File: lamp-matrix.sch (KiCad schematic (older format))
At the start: 0 parts

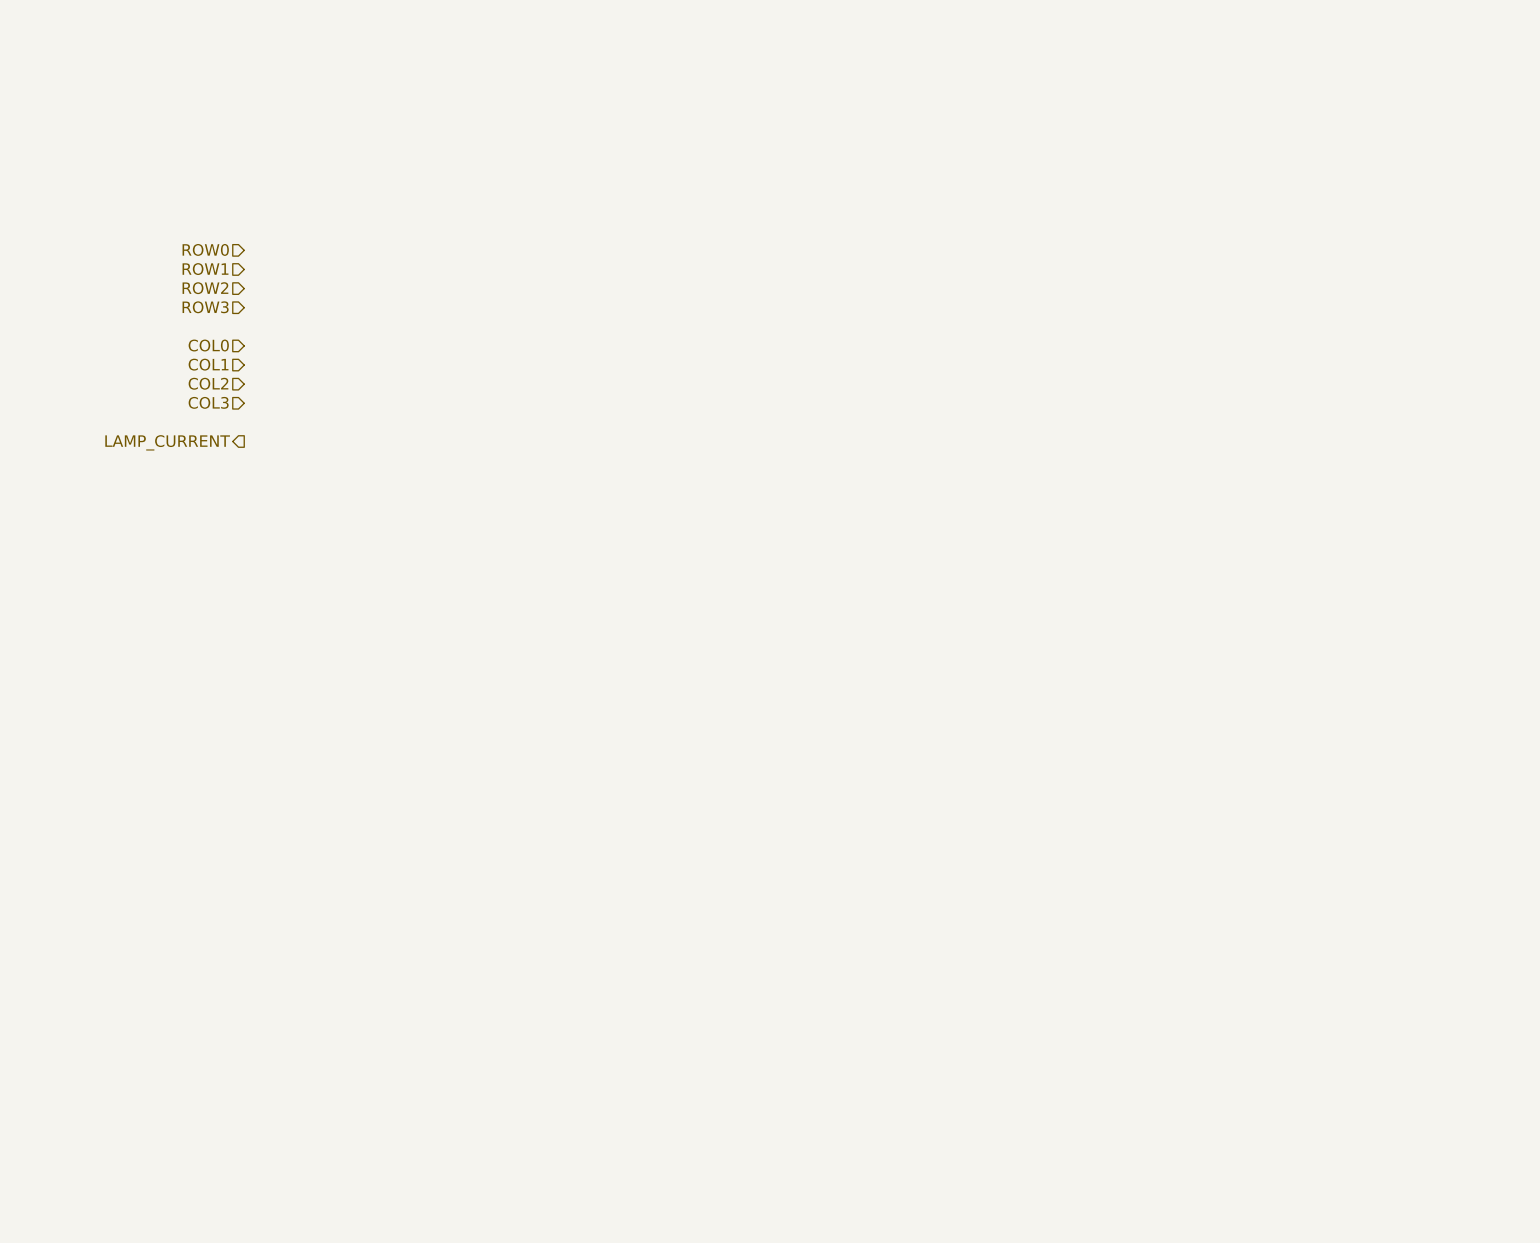
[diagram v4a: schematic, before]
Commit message: Fixed switch matrix to match Mike's sketches Added lamp matrix
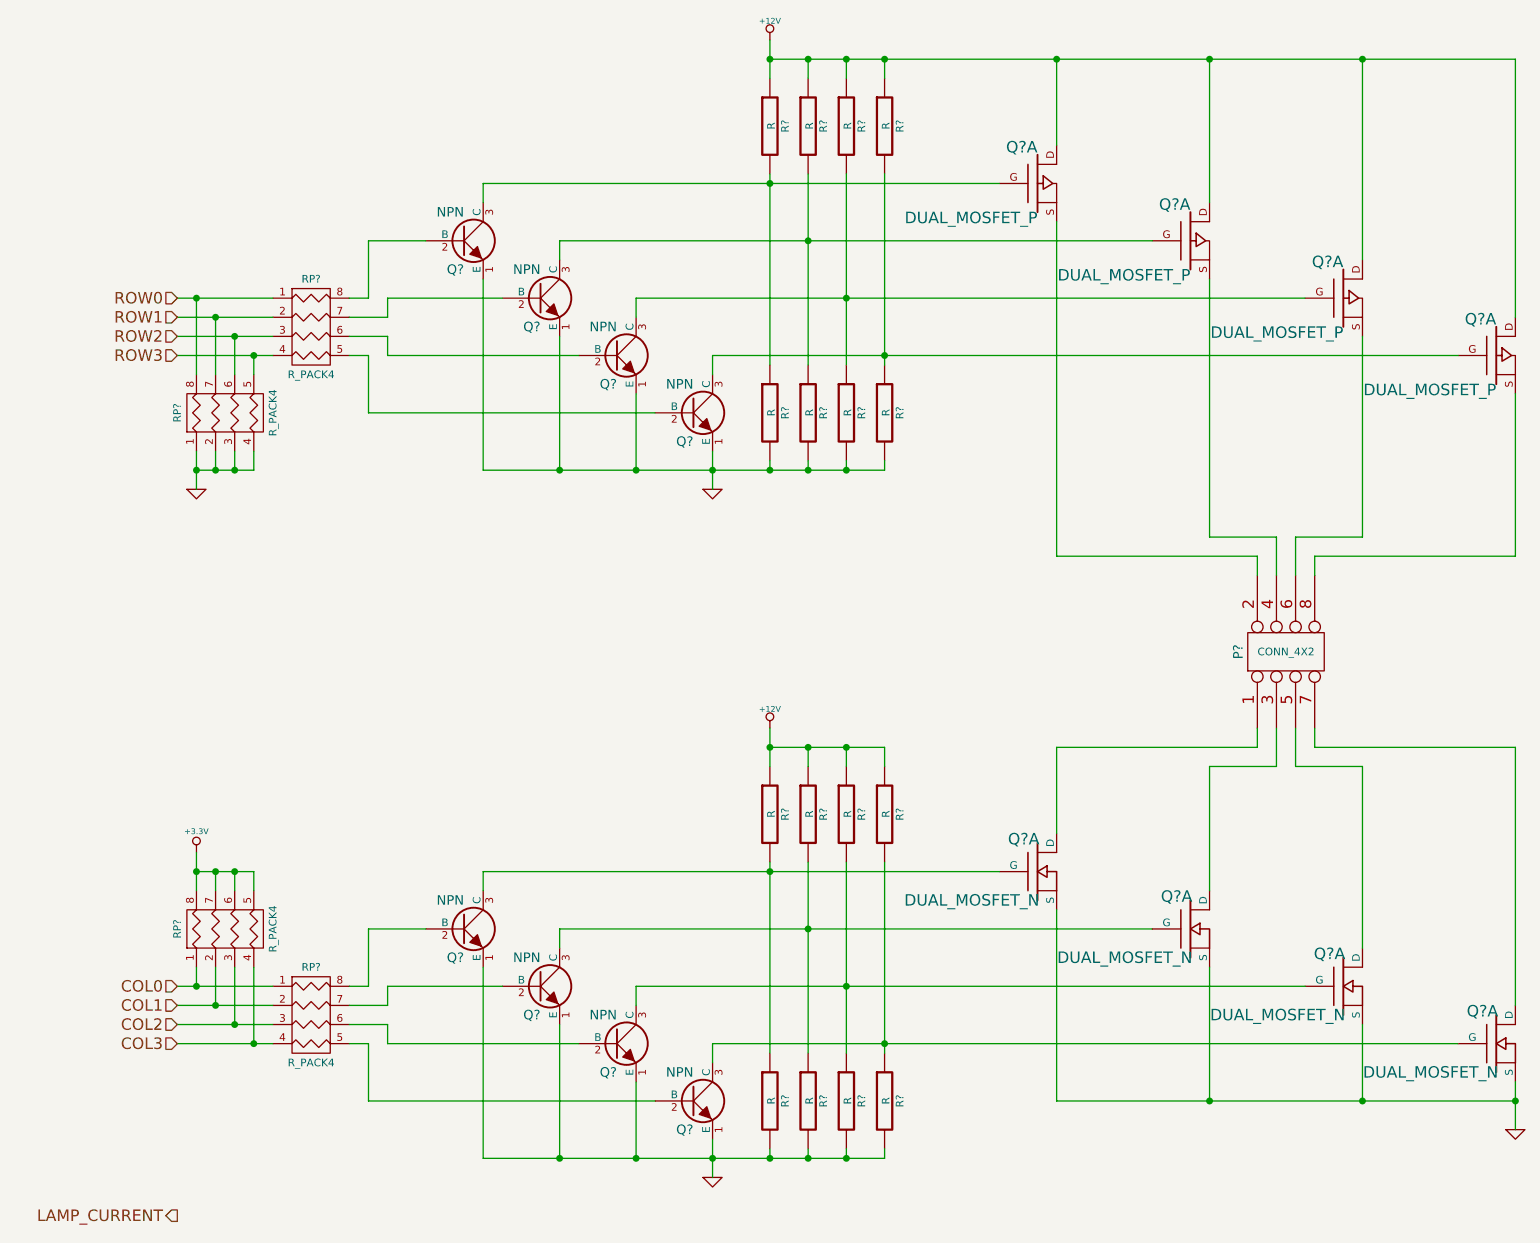
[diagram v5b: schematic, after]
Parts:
- added P?: CONN_4X2, symbol CONN_4X2
- added Q? (x8): NPN, ~, symbol NPN
- added Q? (x4): DUAL_MOSFET_N, ~, symbol DUAL_MOSFET_N
- added Q? (x4): DUAL_MOSFET_P, ~, symbol DUAL_MOSFET_P
- added R? (x16): R, ~, symbol R
- added RP? (x4): R_PACK4, ~, symbol R_PACK4
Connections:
- net COL0: now also RP?.1 (P1), RP?.1 (P1)
- net COL1: now also RP?.2 (P2), RP?.2 (P2)
- net COL2: now also RP?.3 (P3), RP?.3 (P3)
- net COL3: now also RP?.4 (P4), RP?.4 (P4)
- net ROW0: now also RP?.1 (P1), RP?.8 (R1)
- net ROW1: now also RP?.2 (P2), RP?.7 (R2)
- net ROW2: now also RP?.3 (P3), RP?.6 (R3)
- net ROW3: now also RP?.4 (P4), RP?.5 (R4)
- new net: Q?.2 (B), RP?.8 (R1) (x2)
- new net: Q?.3 (C), Q?.G1 (G), R?.1, R?.2 (x4)
- new net: Q?.2 (B), RP?.5 (R4) (x2)
- new net: Q?.2 (B), RP?.6 (R3) (x2)
- new net: Q?.2 (B), RP?.7 (R2) (x2)
- new net: P?.3, Q?.D1 (D)
- new net: P?.1, Q?.D1 (D)
- new net: P?.5, Q?.D1 (D)
- new net: P?.7, Q?.D1 (D)
- new net: P?.2, Q?.S
- new net: P?.4, Q?.S
- new net: P?.6, Q?.S
- new net: P?.8, Q?.S
- new net: Q?.3 (C), Q?.G, R?.1, R?.2 (x4)
- new net +12V: Q?.D, Q?.D, Q?.D, Q?.D, R?.1, R?.1, R?.1, R?.1, R?.1, R?.1, R?.1, R?.1
- new net +3.3V: RP?.5 (R4), RP?.6 (R3), RP?.7 (R2), RP?.8 (R1)
- new net GND: Q?.1 (E), Q?.1 (E), Q?.1 (E), Q?.1 (E), Q?.1 (E), Q?.1 (E), Q?.1 (E), Q?.1 (E), Q?.S1 (S), Q?.S1 (S), Q?.S1 (S), Q?.S1 (S), R?.2, R?.2, R?.2, R?.2, R?.2, R?.2, R?.2, R?.2, RP?.1 (P1), RP?.2 (P2), RP?.3 (P3), RP?.4 (P4)
